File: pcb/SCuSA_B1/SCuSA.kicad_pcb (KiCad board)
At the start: 2 copper layers, 51 x 42 mm, 79 parts, among them J101 USB4135-GF-A, J102 JST_S2B-PH-K-x, J103 Binding_Post_PKI_10_A_Au, J104 Binding_Post_PKI_10_A_Au, J105 SMA_Straight_Jack_Female, J107 77311-118-02LF, J108 77311-118-02LF, Q101 DMN2041LSD, SW101 JS202011CQN, SW102 JS202011CQN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

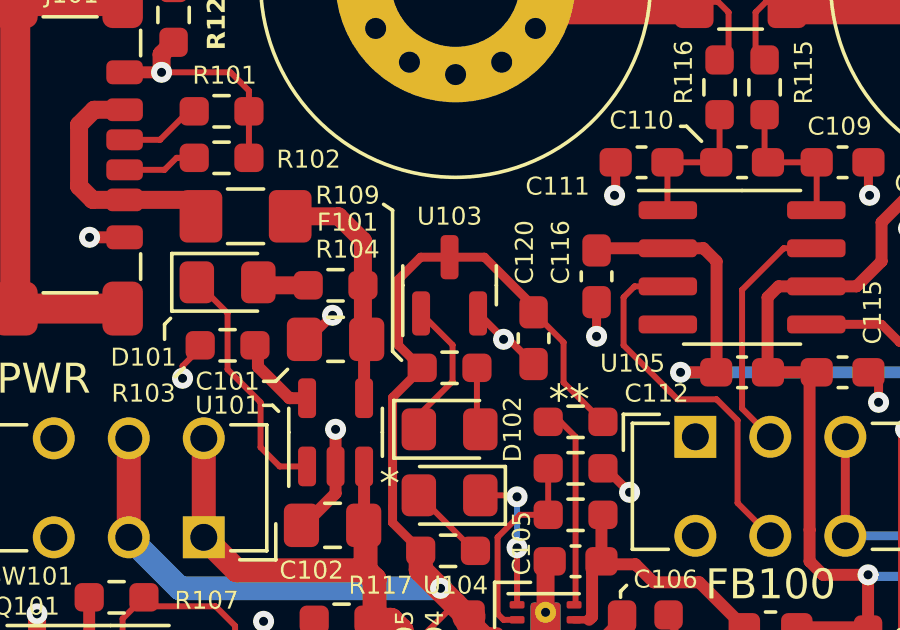
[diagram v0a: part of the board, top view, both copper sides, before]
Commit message: Fix TLV803EA30DBZR (non-R pinout)
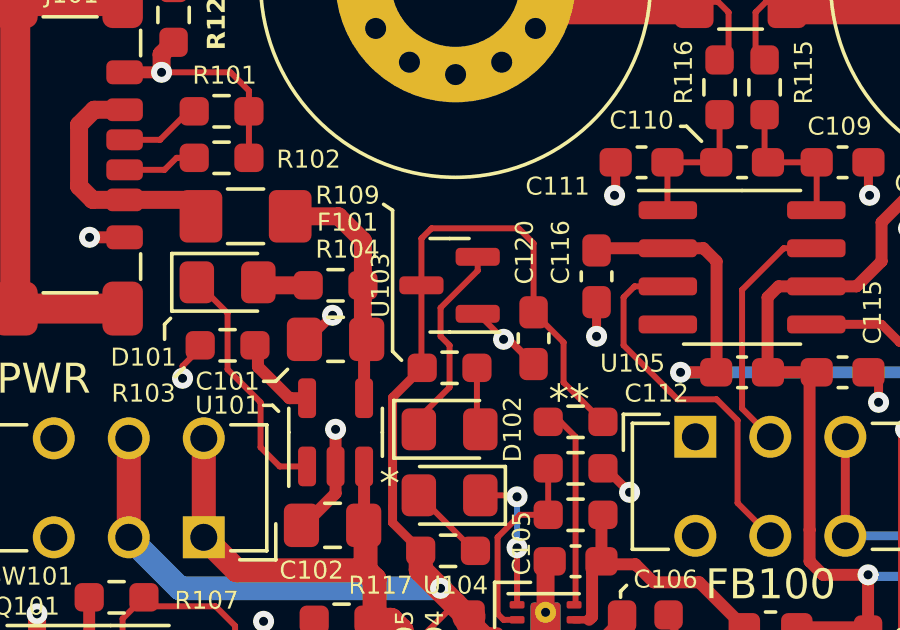
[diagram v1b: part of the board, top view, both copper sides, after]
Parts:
- turned U103 to 180 degrees
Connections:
- U103 pad 1: Net-(D102-K) -> GND
- U103 pad 2: GND -> Net-(D102-K)
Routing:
- net Net-(D102-K): track 4.76 -> 6.81 mm
- net /VBat_SW: track 66.4 -> 68.4 mm
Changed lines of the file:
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@@
   )
   (footprint "Package_TO_SOT_SMD:SOT-23" (layer "F.Cu")
-    (at 127.8 79.1 90)
+    (at 127.8 79.1 180)
     (descr "SOT, 3 Pin (https://www.jedec.org/system/files/docs/to-236h.pdf variant AB), generated with kicad-footprint-generator ipc_gullwing_generator.py")
     (tags "SOT TO_SOT_SMD")
@@
     (property "ki_keywords" "supply voltage supervisor")
     (attr smd)
-    (fp_text reference "U103" (at 2.3 0 180) (layer "F.SilkS")
-        (effects (font (size 0.6 0.6) (thickness 0.1)))
-    )
-    (fp_text value "TLV803EA30DBZR" (at 0 2.4 90) (layer "F.Fab")
-        (effects (font (size 1 1) (thickness 0.15)))
-    )
-    (fp_text user "${REFERENCE}" (at 0 0 90) (layer "F.Fab")
+    (fp_text reference "U103" (at 2.3 0 90) (layer "F.SilkS")
+        (effects (font (size 0.6 0.6) (thickness 0.1)))
+    )
+    (fp_text value "TLV803EA30DBZR" (at 0 2.4) (layer "F.Fab")
+        (effects (font (size 1 1) (thickness 0.15)))
+    )
+    (fp_text user "${REFERENCE}" (at 0 0) (layer "F.Fab")
         (effects (font (size 0.32 0.32) (thickness 0.05)))
     )
@@
     (fp_line (start 0.65 1.45) (end -0.65 1.45)
       (stroke (width 0.1) (type solid)) (layer "F.Fab"))
-    (pad "1" smd roundrect (at -0.9375 -0.95 90) (size 1.475 0.6) (layers "F.Cu" "F.Paste" "F.Mask") (roundrect_rratio 0.25)
+    (pad "1" smd roundrect (at -0.9375 -0.95 180) (size 1.475 0.6) (layers "F.Cu" "F.Paste" "F.Mask") (roundrect_rratio 0.25)
+      (net 2 "GND") (pinfunction "GND") (pintype "power_in"))
+    (pad "2" smd roundrect (at -0.9375 0.95 180) (size 1.475 0.6) (layers "F.Cu" "F.Paste" "F.Mask") (roundrect_rratio 0.25)
       (net 13 "Net-(D102-K)") (pinfunction "~{RESET}") (pintype "output"))
-    (pad "2" smd roundrect (at -0.9375 0.95 90) (size 1.475 0.6) (layers "F.Cu" "F.Paste" "F.Mask") (roundrect_rratio 0.25)
-      (net 2 "GND") (pinfunction "GND") (pintype "power_in"))
-    (pad "3" smd roundrect (at 0.9375 0 90) (size 1.475 0.6) (layers "F.Cu" "F.Paste" "F.Mask") (roundrect_rratio 0.25)
+    (pad "3" smd roundrect (at 0.9375 0 180) (size 1.475 0.6) (layers "F.Cu" "F.Paste" "F.Mask") (roundrect_rratio 0.25)
       (net 1 "/VBat_SW") (pinfunction "VDD") (pintype "power_in"))
     (model "${KICAD6_3DMODEL_DIR}/Package_TO_SOT_SMD.3dshapes/SOT-23.wrl"
@@
   (segment (start 134.8 98.3) (end 134.2 98.9) (width 0.2) (layer "F.Cu") (net 1))
   (segment (start 136.25 92) (end 136.25 92.25) (width 0.2) (layer "F.Cu") (net 1))
-  (segment (start 126.1 78.9) (end 126.8375 78.1625) (width 0.3) (layer "F.Cu") (net 1))
   (segment (start 126.9 90.8) (end 127.975 89.725) (width 0.2) (layer "F.Cu") (net 1))
   (segment (start 125.9 86.5) (end 125.9 82.8375) (width 0.3) (layer "F.Cu") (net 1))
+  (segment (start 130.1 77.2) (end 130.6 77.7) (width 0.2) (layer "F.Cu") (net 1))
   (segment (start 131.6 81) (end 131.6 82.3375) (width 0.2) (layer "F.Cu") (net 1))
   (segment (start 130.6 80) (end 131.6 81) (width 0.2) (layer "F.Cu") (net 1))
-  (segment (start 128.9625 78.1625) (end 130.6 79.8) (width 0.3) (layer "F.Cu") (net 1))
-  (segment (start 126.1 81.1) (end 126.1 78.9) (width 0.3) (layer "F.Cu") (net 1))
   (segment (start 129.4 90.7) (end 129.0625 90.7) (width 0.4) (layer "F.Cu") (net 1))
-  (segment (start 127.8 78.1625) (end 128.9625 78.1625) (width 0.3) (layer "F.Cu") (net 1))
+  (segment (start 126.8625 77.5375) (end 127.2 77.2) (width 0.2) (layer "F.Cu") (net 1))
   (segment (start 136 91.75) (end 136.25 92) (width 0.2) (layer "F.Cu") (net 1))
   (segment (start 125.9 87.0125) (end 126.8375 87.95) (width 0.3) (layer "F.Cu") (net 1))
+  (segment (start 130.6 77.7) (end 130.6 80) (width 0.2) (layer "F.Cu") (net 1))
+  (segment (start 126.8625 81.825) (end 126.8875 81.85) (width 0.2) (layer "F.Cu") (net 1))
+  (segment (start 126.8625 79.1) (end 126.8625 77.5375) (width 0.2) (layer "F.Cu") (net 1))
   (segment (start 130.05 90.75) (end 129.45 90.75) (width 0.25) (layer "F.Cu") (net 1))
   (segment (start 125.9 82.8375) (end 126.8875 81.85) (width 0.3) (layer "F.Cu") (net 1))
   (segment (start 129.45 90.75) (end 129.4 90.7) (width 0.25) (layer "F.Cu") (net 1))
-  (segment (start 126.8375 78.1625) (end 127.8 78.1625) (width 0.3) (layer "F.Cu") (net 1))
   (segment (start 135.7 98.3) (end 134.8 98.3) (width 0.2) (layer "F.Cu") (net 1))
+  (segment (start 126.8625 79.1) (end 126.8625 81.825) (width 0.2) (layer "F.Cu") (net 1))
   (segment (start 127.975 89.725) (end 128.3875 90.1375) (width 0.8) (layer "F.Cu") (net 1))
   (segment (start 130.6 79.8) (end 130.6 80) (width 0.3) (layer "F.Cu") (net 1))
   (segment (start 128.5 90.1375) (end 128.3875 90.1375) (width 1) (layer "F.Cu") (net 1))
   (segment (start 125.9 86.5) (end 125.9 87.0125) (width 0.3) (layer "F.Cu") (net 1))
+  (segment (start 127.2 77.2) (end 130.1 77.2) (width 0.2) (layer "F.Cu") (net 1))
   (segment (start 134.2 98.9) (end 128.2 98.9) (width 0.2) (layer "F.Cu") (net 1))
   (segment (start 136 91.282106) (end 136 91.75) (width 0.2) (layer "F.Cu") (net 1))
@@
   (segment (start 126.9 97.6) (end 126.9 90.8) (width 0.2) (layer "F.Cu") (net 1))
   (segment (start 131.6 82.3375) (end 132.9125 83.65) (width 0.2) (layer "F.Cu") (net 1))
-  (segment (start 126.85 81.85) (end 126.1 81.1) (width 0.3) (layer "F.Cu") (net 1))
   (segment (start 129.0625 90.7) (end 128.5 90.1375) (width 0.4) (layer "F.Cu") (net 1))
   (segment (start 126.8375 87.95) (end 126.8375 88.5875) (width 0.8) (layer "F.Cu") (net 1))
@@
   (segment (start 129.4 91.3) (end 129.0625 91.3) (width 0.4) (layer "F.Cu") (net 2))
   (segment (start 138.4 92.8) (end 139.8 92.8) (width 0.4) (layer "F.Cu") (net 2))
-  (segment (start 129.6 80.8875) (end 128.75 80.0375) (width 0.25) (layer "F.Cu") (net 2))
   (segment (start 118.2 72) (end 118.2 71.4) (width 0.6) (layer "F.Cu") (net 2))
   (segment (start 115.8 77.5) (end 116.9675 77.5) (width 0.4) (layer "F.Cu") (net 2))
@@
   (segment (start 153 82.6375) (end 153 82.6) (width 0.2) (layer "F.Cu") (net 2))
   (segment (start 121.1125 72.6125) (end 121.1125 73.3) (width 0.2) (layer "F.Cu") (net 2))
+  (segment (start 128.75 80.05) (end 129.6 80.9) (width 0.2) (layer "F.Cu") (net 2))
   (segment (start 132.7 79.6625) (end 132.7 80.8) (width 0.3) (layer "F.Cu") (net 2))
   (segment (start 155.06 80.54) (end 155.46 80.54) (width 0.2) (layer "F.Cu") (net 2))
@@
   (segment (start 136.3 93.7) (end 137.2 92.8) (width 0.4) (layer "F.Cu") (net 2))
   (segment (start 141.7625 76.0625) (end 141.8 76.1) (width 0.3) (layer "F.Cu") (net 2))
+  (segment (start 128.7375 80.05) (end 128.75 80.05) (width 0.2) (layer "F.Cu") (net 2))
   (segment (start 124 86.0375) (end 124 85.1375) (width 0.4) (layer "F.Cu") (net 2))
   (segment (start 133 85.2) (end 133.8 86) (width 0.3) (layer "F.Cu") (net 2))
@@
   (segment (start 135.2 96.9) (end 135.2 95.4625) (width 0.4) (layer "F.Cu") (net 12))
   (segment (start 136.5375 96.8) (end 138.4 96.8) (width 0.4) (layer "F.Cu") (net 12))
-  (segment (start 127.9 82.3) (end 127.9 81.0875) (width 0.2) (layer "F.Cu") (net 13))
-  (segment (start 126.775 83.425) (end 127.9 82.3) (width 0.2) (layer "F.Cu") (net 13))
-  (segment (start 127.9 81.0875) (end 126.85 80.0375) (width 0.2) (layer "F.Cu") (net 13))
-  (segment (start 126.775 83.9) (end 126.775 83.425) (width 0.2) (layer "F.Cu") (net 13))
+  (segment (start 128.7375 78.6125) (end 128.7375 78.15) (width 0.2) (layer "F.Cu") (net 13))
+  (segment (start 127.8 82.5) (end 127.8 81.1) (width 0.2) (layer "F.Cu") (net 13))
+  (segment (start 127.5 80.8) (end 127.5 79.85) (width 0.2) (layer "F.Cu") (net 13))
+  (segment (start 126.775 83.9) (end 126.775 83.525) (width 0.2) (layer "F.Cu") (net 13))
+  (segment (start 127.5 79.85) (end 128.7375 78.6125) (width 0.2) (layer "F.Cu") (net 13))
+  (segment (start 127.8 81.1) (end 127.5 80.8) (width 0.2) (layer "F.Cu") (net 13))
+  (segment (start 126.775 83.525) (end 127.8 82.5) (width 0.2) (layer "F.Cu") (net 13))
   (segment (start 128.7125 83.7875) (end 128.825 83.9) (width 0.2) (layer "F.Cu") (net 14))
   (segment (start 128.7125 81.85) (end 128.7125 83.7875) (width 0.2) (layer "F.Cu") (net 14))

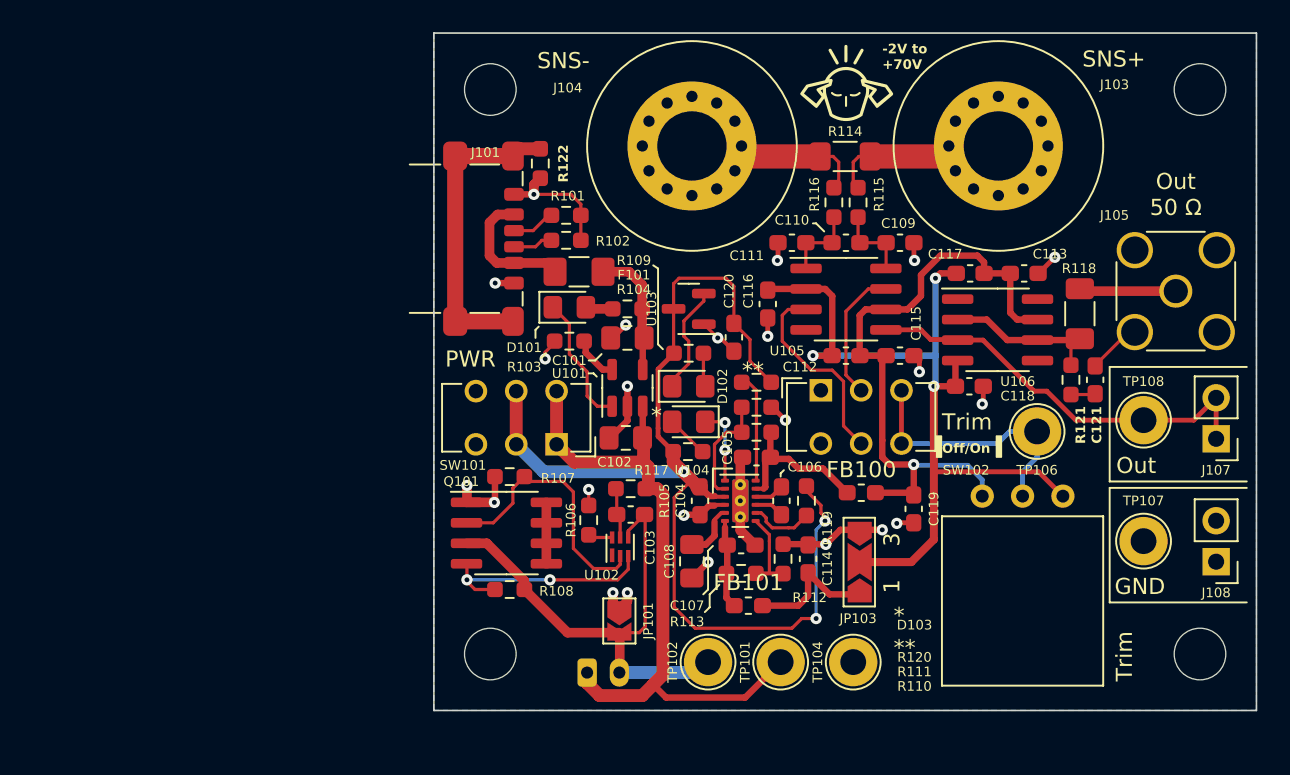
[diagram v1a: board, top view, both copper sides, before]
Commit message: Change charge pump
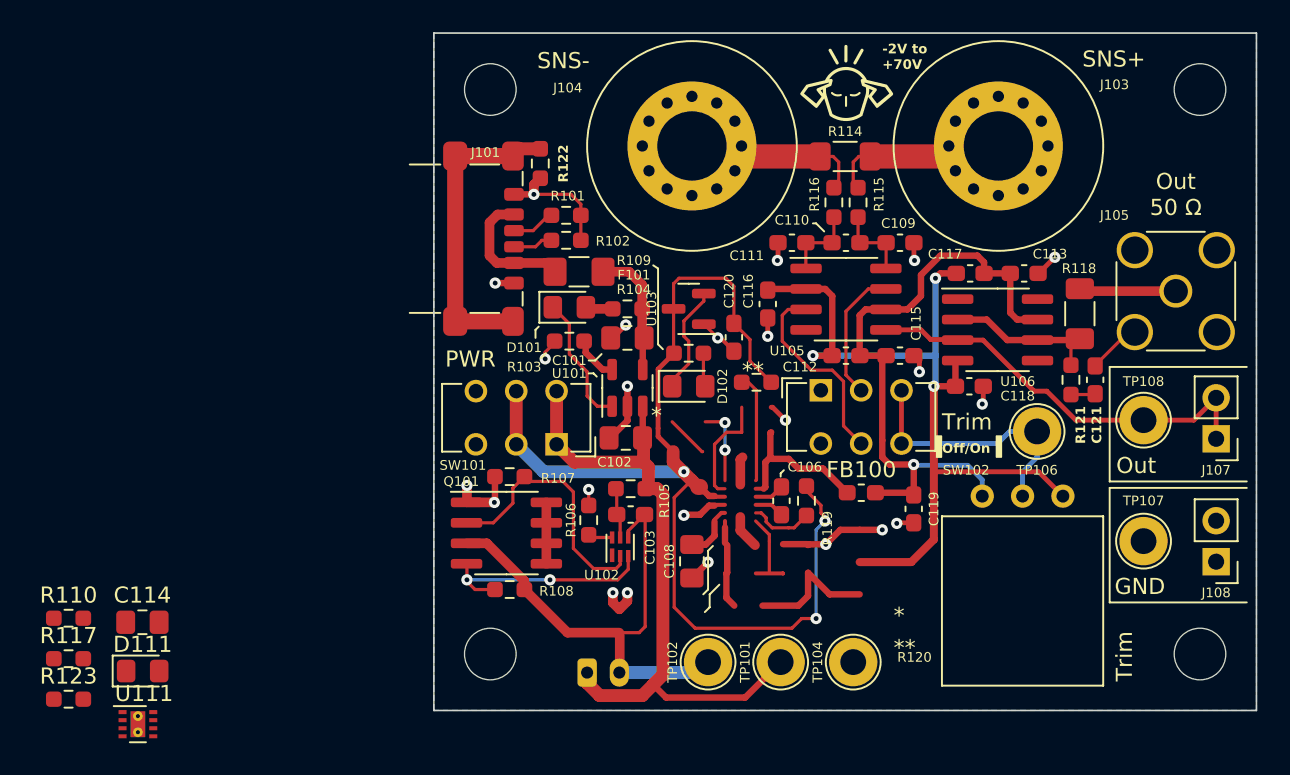
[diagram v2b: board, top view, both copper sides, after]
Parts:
- removed C104, C105, C107: 2.2uF,25V,X7R,0603, Capacitor_SMD:C_0603_1608Metric_Pad1.08x0.95mm_HandSolder
- removed D103: 150080GS75000, LED_SMD:LED_0805_2012Metric_Pad1.15x1.40mm_HandSolder
- removed FB101: 742792620, Inductor_SMD:L_0603_1608Metric_Pad1.05x0.95mm_HandSolder
- removed JP101: SolderJumper_2_Open, Jumper:SolderJumper-2_P1.3mm_Open_TrianglePad1.0x1.5mm
- removed JP103: SolderJumper_3_Open, Jumper:SolderJumper-3_P2.0mm_Open_TrianglePad1.0x1.5mm_NumberLabels
- removed R111, R112: 68k,0603, Resistor_SMD:R_0603_1608Metric_Pad0.98x0.95mm_HandSolder
- removed R113: 47k,0603, Resistor_SMD:R_0603_1608Metric_Pad0.98x0.95mm_HandSolder
- removed U104: LM27762, Package_SON_User:WSON-12-1EP_3x2mm_P0.5mm_EP1x2.65_ThermalVias
- added D111: 150080GS75000, LED_SMD:LED_0805_2012Metric_Pad1.15x1.40mm_HandSolder, F.Cu at (93.9, 101.6)
- added R123: 0R,0603, Resistor_SMD:R_0603_1608Metric_Pad0.98x0.95mm_HandSolder, F.Cu at (89.3, 103.3)
- added U111: LM2775DSG, Package_SON:WSON-8-1EP_2x2mm_P0.5mm_EP0.9x1.6mm_ThermalVias, F.Cu at (93.7, 104.8)
- C114: value 1uF,16V,X7R,0603 -> 4.7uF,25V,X7R,0805; footprint Capacitor_SMD:C_0603_1608Metric_Pad1.08x0.95mm_HandSolder -> Capacitor_SMD:C_0805_2012Metric_Pad1.18x1.45mm_HandSolder
- R103: value 10k,0603 -> 4.7k,0603
- R104: value 470R,0603 -> 1.2k,0603
- R110: value 120k,0603 -> 0R,0603
- moved R110 44.2 mm to (89.3, 98.3), turned to 0 degrees
- moved C114 41.5 mm to (93.9, 98.5), turned to 0 degrees
- moved R117 40.5 mm to (89.3, 100.8), turned to 0 degrees
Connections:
- C108 pad 1: Net-(U104-CP) -> Net-(U111-VOUT)
- C112 pad 2: -Vx -> GND
- C114 pad 1: /-2V_filt -> /VBat_SW
- C116 pad 2: -Vx -> GND
- C117 pad 1: -Vx -> GND
- C118 pad 1: -Vx -> GND
- FB100 pad 1: Net-(U104-OUT+) -> Net-(U111-VOUT)
- R110 pad 1: Net-(U104-OUT+) -> GND
- R110 pad 2: Net-(U104-FB+) -> /Cell-
- R119 pad 2: Net-(U104-EN-) -> Net-(U111-PFM)
- R120 pad 1: /VBat_SW -> GND
- R120 pad 2: Net-(U104-EN+) -> Net-(U111-PFM)
- RV101 pad 3: -Vx -> GND
- U105 pad 2: -Vx -> GND
- U106 pad 4: -Vx -> GND
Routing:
- net -Vx: track 51.2 -> 0.00 mm, vias 3 -> 0
- net GND: track 52.6 -> 103.7 mm, vias 23 -> 26
- net (no net): track 0.00 -> 33.4 mm, vias 0 -> 2
- net Net-(U111-VOUT): track 0.00 -> 13.3 mm
- net Net-(U111-PFM): track 0.00 -> 10.7 mm
- net Net-(U104-OUT+): track 9.87 -> 0.00 mm
- net /-2V_filt: track 8.27 -> 0.00 mm
- net Net-(U104-FB+): track 6.83 -> 0.00 mm
- net Net-(U104-EN+): track 6.74 -> 0.00 mm
- net /-2V: track 5.53 -> 0.00 mm
- net Net-(U104-FB-): track 5.24 -> 0.00 mm
- net /PGOOD: track 4.85 -> 0.00 mm, vias 2 -> 0
- net Net-(U104-EN-): track 4.00 -> 0.00 mm
- net Net-(U104-CP): track 3.45 -> 0.00 mm
- net Net-(D111-A): track 2.65 -> 0.00 mm

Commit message: Change voltage supervisor
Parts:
- C119: value 1uF,16V,X7R,0603 -> 4.7uF,25V,X7R,0805; footprint Capacitor_SMD:C_0603_1608Metric_Pad1.08x0.95mm_HandSolder -> Capacitor_SMD:C_0805_2012Metric_Pad1.18x1.45mm_HandSolder
- U103: value TLV803EA30DBZR -> BD4836G-xx; footprint Package_TO_SOT_SMD:SOT-23 -> Package_TO_SOT_SMD:SOT-23-5
- moved U103 30.0 mm to (97.9, 81.0), turned to 0 degrees
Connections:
- net +3V3 renamed +5V
- U103 pad 1: GND -> Net-(D102-K)
- U103 pad 2: Net-(D102-K) -> /VBat_SW
- U103 pad 3: /VBat_SW -> GND
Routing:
- net /VBat_SW: track 68.4 -> 57.7 mm
- net Net-(D102-K): track 6.81 -> 0.38 mm
- net GND: track 103.7 -> 102.5 mm

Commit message: Edit PCB layout
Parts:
- removed TP101: TestPoint_5010_Red, TestPoint:TestPoint_Loop_D2.60mm_Drill1.6mm_Beaded
- removed TP102, TP104: TestPoint_5011_Black, TestPoint:TestPoint_Loop_D2.60mm_Drill1.6mm_Beaded
- removed TP106: TestPoint_5012_White, TestPoint:TestPoint_Loop_D2.60mm_Drill1.6mm_Beaded
- D101, D102, D111, G***, J103, J104, J105, J107, J108, SW101, SW102, TP107, TP108: moved to B.Cu
- J102: value JST_S2B-PH-K-x -> JST_S2B-PH-SM4-x; footprint Connector_JST:JST_PH_S2B-PH-K_1x02_P2.00mm_Horizontal -> Connector_User:JST_PH_S2B-PH-SM4-TB_1x02-1MP_P2.00mm_Horizontal; moved to F.Cu
- moved R123 45.2 mm to (130.3, 84.1), turned to 180 degrees
- moved U111 39.9 mm to (129.9, 88.1), turned to -90 degrees
- moved C114 35.2 mm to (127.5, 88.1), turned to 90 degrees
- moved D111 34.2 mm to (121.6, 81.4), turned to 180 degrees
- moved R117 32.6 mm to (116.3, 82.5)
- moved U103 30.0 mm to (127.8, 79.4), turned to 90 degrees
- moved R110 27.9 mm to (116.7, 92.7), turned to -90 degrees
- moved FB100 8.35 mm to (130.5, 92.9)
- moved C119 8.25 mm to (133.5, 91.7), turned to 90 degrees
- moved D102 7.66 mm to (121.6, 79.4), turned to 180 degrees
- moved C106 6.22 mm to (130.3, 85.7), turned to 0 degrees
- moved G*** 6.10 mm to (137.4, 71.4), turned to 180 degrees
- moved R120 5.33 mm to (132.9, 88.9)
- moved SW102 4.92 mm to (140.9, 84.3), turned to 180 degrees
- moved C108 4.76 mm to (130.5, 90.7), turned to 0 degrees
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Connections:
- RV101 pad 2: Net-(SW102A-C) -> Net-(SW102A-A)
- SW102 pad 1: GND -> Net-(SW102A-A)
- SW102 pad 3: Net-(SW102A-C) -> GND
- SW102 pad 4: GND -> Net-(SW102A-A)
- SW102 pad 6: Net-(SW102A-C) -> GND
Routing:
- net /VBat_SW: track 57.7 -> 17.4 mm, vias 3 -> 1
- net GND: track 102.5 -> 62.5 mm, vias 26 -> 19
- net (no net): track 33.4 -> 0.00 mm, vias 2 -> 0
- net Net-(SW102A-C): track 16.4 -> 0.00 mm
- net /VBat: track 42.2 -> 27.7 mm
- net Net-(U111-VOUT): track 13.3 -> 0.00 mm
- net Net-(U111-PFM): track 10.7 -> 0.00 mm
- net Net-(SW102A-A): track 0.00 -> 9.60 mm
- net /Cell-: track 31.0 -> 22.2 mm, vias 0 -> 2
- net +5V: track 39.4 -> 31.9 mm, vias 1 -> 0
- net Net-(D102-A): track 2.10 -> 0.00 mm
- net Net-(U111-C1-): track 1.85 -> 0.00 mm
- net Net-(U111-C1+): track 1.85 -> 0.00 mm
- net Net-(Q101A-G1): track 16.3 -> 17.8 mm
- net Net-(D101-K): track 8.19 -> 7.66 mm
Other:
- board text added: "Charging"
- board text added: "Low Bat"
- board text added: "Max. -2V to +70V"
- board text added: "Power"
- board text added: "Power On/Off"
- board text added: "SCuSA Scope Current Sense Amplifier Rev B1, by fl0m0"
- board text added: "Trim +←→-"
- board text added: "Trim On/Off"
- board text removed: "-2V to +70V"
- board text removed: "Off/On"
- board text removed: "Scope Current Sense Amplifier SCuSA - Rev B1 by fl0m0"
- board text removed: "Trim"

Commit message: Edit PCB layout
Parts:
- removed C117, C118: 100nF,16V,X7R,0603, Capacitor_SMD:C_0603_1608Metric_Pad1.08x0.95mm_HandSolder
- moved C120 3.02 mm to (127.8, 82.0), turned to 180 degrees
- moved R109 2.85 mm to (126.9, 79.5), turned to 90 degrees
- moved U103 2.10 mm to (129.9, 79.5), turned to 0 degrees
- moved R104 1.66 mm to (124.9, 77.7), turned to 90 degrees
- moved D101 0.51 mm to (121.5, 76.9)
- moved D102 0.32 mm to (121.5, 79.1)
- moved R117 0.22 mm to (116.5, 82.4), turned to 180 degrees
- moved D111 0.14 mm to (121.5, 81.3)
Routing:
- net /VBat_SW: track 17.4 -> 51.5 mm, vias 1 -> 2
- net +5V: track 31.9 -> 44.1 mm
- net Net-(D102-A): track 0.00 -> 8.18 mm, vias 0 -> 1
- net Net-(D102-K): track 0.00 -> 6.70 mm, vias 0 -> 1
- net Net-(D101-K): track 7.66 -> 12.5 mm, vias 0 -> 1
- net Net-(D101-A): track 1.70 -> 5.87 mm, vias 0 -> 1
- net Net-(U111-VOUT): track 0.00 -> 3.99 mm
- net Net-(U111-OUTDIS): track 0.00 -> 3.60 mm
- net Net-(D111-A): track 0.00 -> 3.52 mm, vias 0 -> 1
- net Net-(SW102A-A): track 9.60 -> 12.9 mm
- net Net-(U111-PFM): track 0.00 -> 3.00 mm
- net GND: track 62.5 -> 64.9 mm, vias 19 -> 21
- net Net-(U111-C1-): track 0.00 -> 1.87 mm
- net Net-(U111-C1+): track 0.00 -> 1.54 mm
- net /VBus: track 8.07 -> 7.20 mm
- added copper zone on F.Cu, net GND
